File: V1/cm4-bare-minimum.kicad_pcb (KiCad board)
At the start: 2 copper layers, 120 x 120 mm, 59 parts, among them J1 Molex 470531000, J2 USB_OTG, J3 THD-02-R, J4 Micro_SD_Card_Det, J5 USB4105-GF-A, J6 Conn_01x03, J7 Conn_01x03, J8 THD-20-R, J9 MDT320M03001, U1 TPD2EUSB30, U2 EMC2301-1-ACZL-TR, U3 MagJack-A70-112-331N126, U4 RT9742GGJ5, U5 74LVC1G07SE-7, U6 MP1470

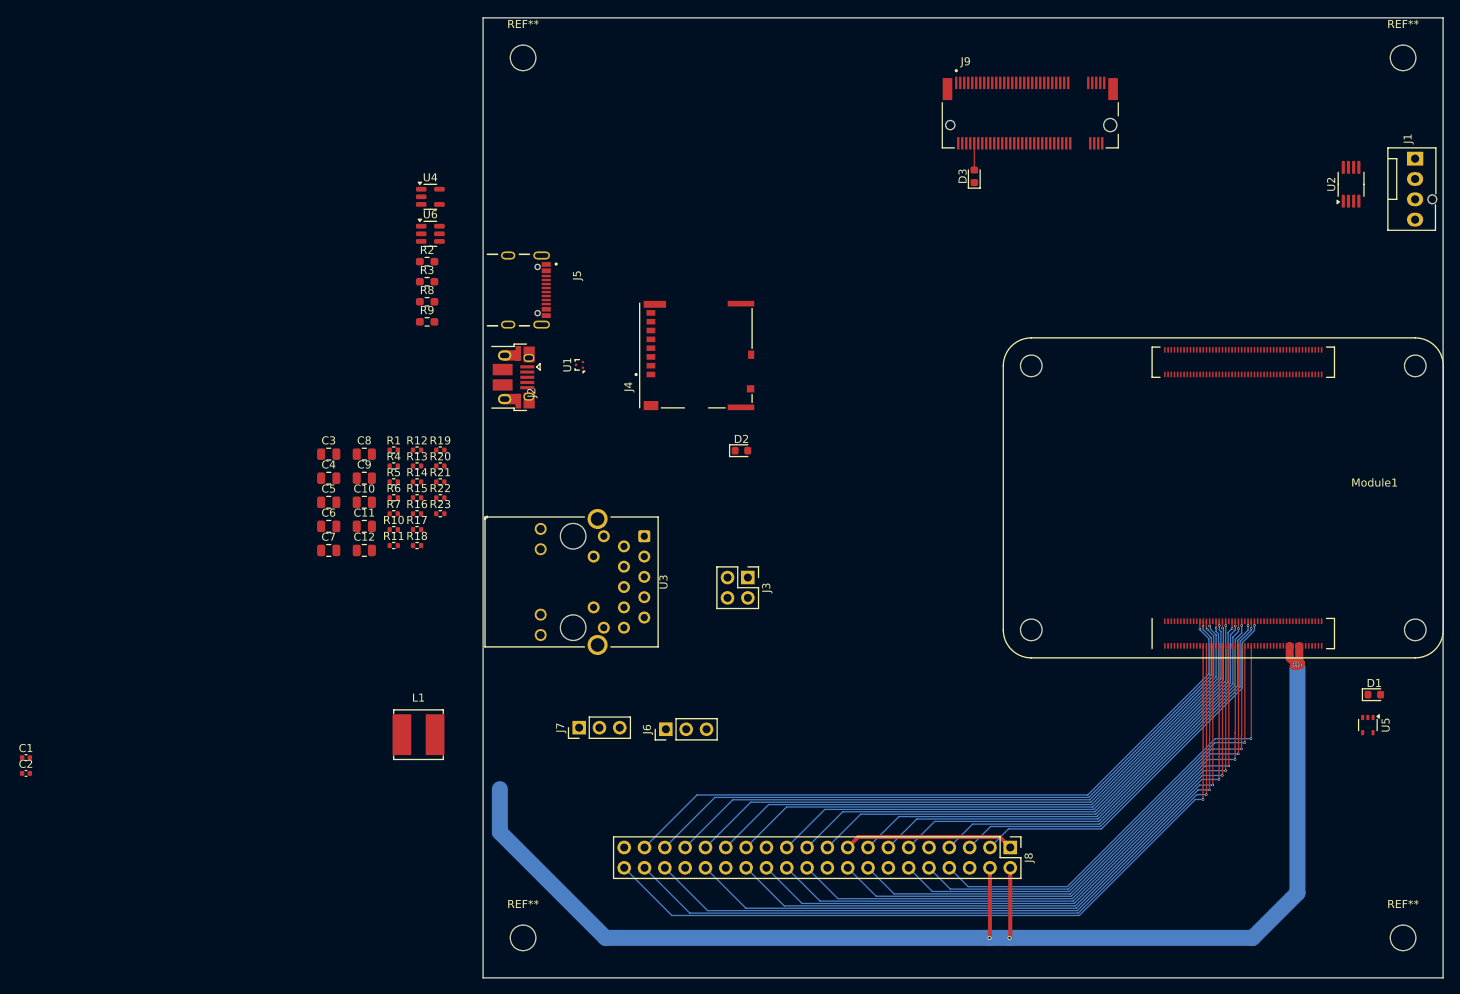
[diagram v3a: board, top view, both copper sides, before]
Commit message: Housekeeping, board size 120mmx40mm
V1 requirements are fulfilled, Connections are remaining in PCB layout, Performed Cleanup of repo so it only has the V1 Project.
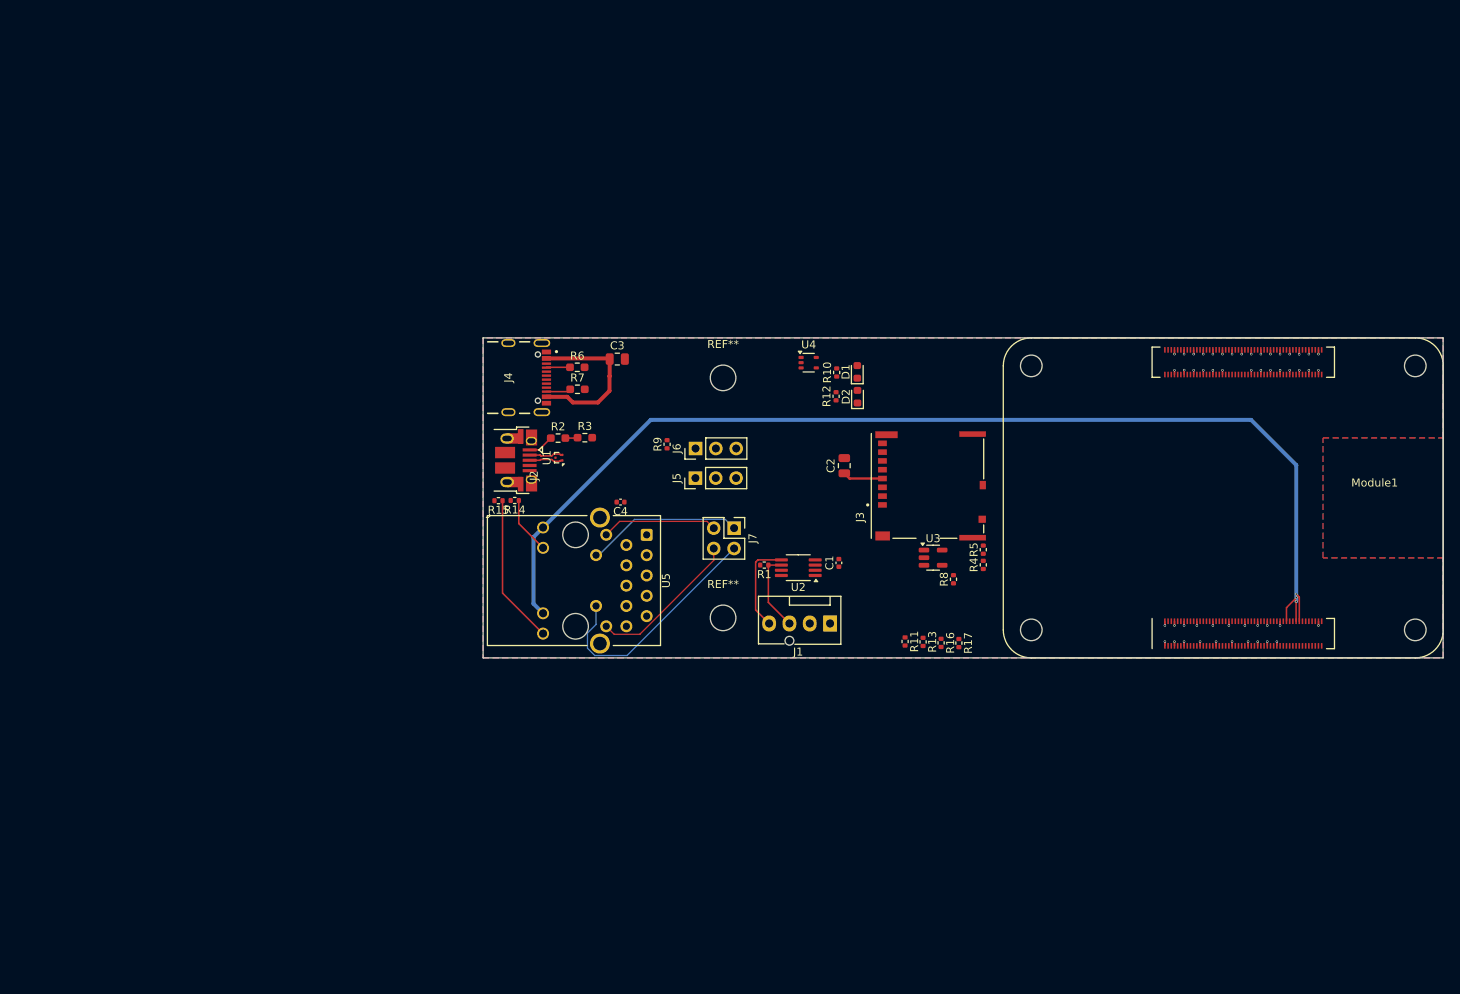
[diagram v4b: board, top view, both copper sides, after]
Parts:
- removed C10, C12, C6: 10u, Capacitor_SMD:C_0805_2012Metric
- removed C11, C7: 0.1u, Capacitor_SMD:C_0805_2012Metric
- removed C5: 13p, Capacitor_SMD:C_0805_2012Metric
- removed C8: 1u, Capacitor_SMD:C_0805_2012Metric
- removed C9: 10p, Capacitor_SMD:C_0805_2012Metric
- removed D3: LED Red, LED_SMD:LED_0603_1608Metric
- removed J8: THD-20-R, Connector_PinHeader_2.54mm:PinHeader_2x20_P2.54mm_Vertical
- removed J9: MDT320M03001, MDT320M03001:AMPHENOL_MDT320M03001
- removed L1: SRN6045TA-4R7Y, Inductor_SMD:L_Bourns_SRN6045TA
- removed R18: NC, Resistor_SMD:R_0402_1005Metric
- removed R19: 10, Resistor_SMD:R_0402_1005Metric
- removed R20: 40.2k, Resistor_SMD:R_0402_1005Metric
- removed R21: 100k, Resistor_SMD:R_0402_1005Metric
- removed R22: 20k, Resistor_SMD:R_0402_1005Metric
- removed R23: 13k, Resistor_SMD:R_0402_1005Metric
- removed the REF** at (205.0, 155.0)
- removed the REF** at (95.0, 45.0)
- removed U6: MP1470, Package_TO_SOT_SMD:TSOT-23-6
- C2: value 100n -> 10u; footprint Capacitor_SMD:C_0402_1005Metric -> Capacitor_SMD:C_0805_2012Metric
- C4: value 1u -> 100n; footprint Capacitor_SMD:C_0805_2012Metric -> Capacitor_SMD:C_0402_1005Metric
- J3: value THD-02-R -> Micro_SD_Card_Det; footprint Connector_PinHeader_2.54mm:PinHeader_2x02_P2.54mm_Vertical -> CM4IO:SDCARD_MOLEX_503398-1892
- J4: value Micro_SD_Card_Det -> USB4105-GF-A; footprint CM4IO:SDCARD_MOLEX_503398-1892 -> USB4105-GF-A:GCT_USB4105-GF-A
- J5: value USB4105-GF-A -> Conn_01x03; footprint USB4105-GF-A:GCT_USB4105-GF-A -> Connector_PinHeader_2.54mm:PinHeader_1x03_P2.54mm_Vertical
- J7: value Conn_01x03 -> THD-02-R; footprint Connector_PinHeader_2.54mm:PinHeader_1x03_P2.54mm_Vertical -> Connector_PinHeader_2.54mm:PinHeader_2x02_P2.54mm_Vertical
- R10: value 12K 1% -> 1k
- R13: value 1k -> NC
- R14: value NC -> 470R
- R15: value 1k -> 470R
- R4, R5: value 470R -> NC
- R6, R7: value NC -> 5.1k; footprint Resistor_SMD:R_0402_1005Metric -> Resistor_SMD:R_0603_1608Metric_Pad0.98x0.95mm_HandSolder
- R8: value 5.1k -> 12K 1%; footprint Resistor_SMD:R_0603_1608Metric_Pad0.98x0.95mm_HandSolder -> Resistor_SMD:R_0402_1005Metric
- R9: value 5.1k -> NC; footprint Resistor_SMD:R_0603_1608Metric_Pad0.98x0.95mm_HandSolder -> Resistor_SMD:R_0402_1005Metric
- U3: value MagJack-A70-112-331N126 -> RT9742GGJ5; footprint CM4IO:TRJG0926HENL -> Package_TO_SOT_SMD:SOT-23-5
- U4: value RT9742GGJ5 -> 74LVC1G07SE-7; footprint Package_TO_SOT_SMD:SOT-23-5 -> Package_TO_SOT_SMD:SOT-353_SC-70-5
- U5: value 74LVC1G07SE-7 -> MagJack-A70-112-331N126; footprint Package_TO_SOT_SMD:SOT-353_SC-70-5 -> CM4IO:TRJG0926HENL
- moved C2 109.3 mm to (135.2, 96.0), turned to 90 degrees
- moved C1 104.5 mm to (134.5, 108.1), turned to 90 degrees
- moved U5 100.7 mm to (101.6, 110.3)
- moved REF** 93.9 mm to (120.0, 85.0)
- moved J1 93.4 mm to (133.4, 115.7), turned to 180 degrees
- moved U2 84.1 mm to (129.4, 108.7), turned to 180 degrees
- moved D1 76.2 mm to (136.8, 84.2), turned to 90 degrees
- moved R4 74.7 mm to (152.5, 108.4), turned to 90 degrees
- moved R8 74.4 mm to (148.8, 110.2), turned to 90 degrees
- moved R5 74.2 mm to (152.5, 106.5), turned to 90 degrees
- moved R17 69.2 mm to (149.5, 118.2), turned to -90 degrees
- moved R16 67.5 mm to (147.2, 118.1), turned to -90 degrees
- moved R13 67.0 mm to (145.0, 118.0), turned to -90 degrees
- moved R11 65.0 mm to (142.8, 118.0), turned to -90 degrees
- moved R10 58.7 mm to (134.2, 84.3), turned to 90 degrees
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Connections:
- C2 pad 1: Net-(C2-Pad1) -> /SD_PWR
- C3 pad 1: /SD_PWR -> /CM4_5V
- C4 pad 2: Net-(U6-SW) -> GND
- D1 pad 2: /PWR_3V3 -> /CM4_3V3
- D2 pad 2: /PWR_3V3 -> /CM4_3V3
- J3 pad 1: /TR1_TAP -> /SD_DAT2
- J3 pad 2: /TR2_TAP -> /SD_DAT3
- J3 pad 3: /TR0_TAP -> /SD_CMD
- J3 pad 4: /TR3_TAP -> /SD_PWR
- J6 pad 1: /Global_EN -> Net-(J6-Pin_1)
- J6 pad 2: GND -> /nRPIBOOT
- J6 pad 3: /RUN_PG -> GND
- J7 pad 1: Net-(J7-Pin_1) -> /TR1_TAP
- J7 pad 2: /nRPIBOOT -> /TR2_TAP
- J7 pad 3: GND -> /TR0_TAP
- Module1 pad 102: /PCIe_CLK_nREQ -> unconnected-(Module1B-PCIe_CLK_nREQ-Pad102)
- Module1 pad 109: /PCIe_nRST -> unconnected-(Module1B-PCIe_nRST-Pad109)
- Module1 pad 110: /PCIe_CLK_P -> unconnected-(Module1B-PCIe_CLK_P-Pad110)
- Module1 pad 112: /PCIe_CLK_N -> unconnected-(Module1B-PCIe_CLK_N-Pad112)
- Module1 pad 116: /PCIe_RX_P -> unconnected-(Module1B-PCIe_RX_P-Pad116)
- Module1 pad 118: /PCIe_RX_N -> unconnected-(Module1B-PCIe_RX_N-Pad118)
- Module1 pad 122: /PCIe_TX_P -> unconnected-(Module1B-PCIe_TX_P-Pad122)
- Module1 pad 124: /PCIe_TX_N -> unconnected-(Module1B-PCIe_TX_N-Pad124)
- Module1 pad 24: /GPIO26 -> unconnected-(Module1A-GPIO26-Pad24)
- Module1 pad 25: /GPIO21 -> unconnected-(Module1A-GPIO21-Pad25)
- Module1 pad 26: /GPIO19 -> unconnected-(Module1A-GPIO19-Pad26)
- Module1 pad 27: /GPIO20 -> unconnected-(Module1A-GPIO20-Pad27)
- Module1 pad 28: /GPIO13 -> unconnected-(Module1A-GPIO13-Pad28)
- Module1 pad 29: /GPIO16 -> unconnected-(Module1A-GPIO16-Pad29)
- Module1 pad 30: /GPIO6 -> unconnected-(Module1A-GPIO6-Pad30)
- Module1 pad 31: /GPIO12 -> unconnected-(Module1A-GPIO12-Pad31)
- Module1 pad 34: /GPIO5 -> unconnected-(Module1A-GPIO5-Pad34)
- Module1 pad 35: /ID_SC -> unconnected-(Module1A-ID_SC-Pad35)
- Module1 pad 36: /ID_SD -> unconnected-(Module1A-ID_SD-Pad36)
- Module1 pad 37: /GPIO7 -> unconnected-(Module1A-GPIO7-Pad37)
- Module1 pad 38: /GPIO11 -> unconnected-(Module1A-GPIO11-Pad38)
- Module1 pad 39: /GPIO8 -> unconnected-(Module1A-GPIO8-Pad39)
- Module1 pad 40: /GPIO9 -> unconnected-(Module1A-GPIO9-Pad40)
- Module1 pad 41: /GPIO25 -> unconnected-(Module1A-GPIO25-Pad41)
- Module1 pad 44: /GPIO10 -> unconnected-(Module1A-GPIO10-Pad44)
- Module1 pad 45: /GPIO24 -> unconnected-(Module1A-GPIO24-Pad45)
- Module1 pad 46: /GPIO22 -> unconnected-(Module1A-GPIO22-Pad46)
- Module1 pad 47: /GPIO23 -> unconnected-(Module1A-GPIO23-Pad47)
- Module1 pad 48: /GPIO27 -> unconnected-(Module1A-GPIO27-Pad48)
- Module1 pad 49: /GPIO18 -> unconnected-(Module1A-GPIO18-Pad49)
- Module1 pad 50: /GPIO17 -> unconnected-(Module1A-GPIO17-Pad50)
- Module1 pad 51: /GPIO15 -> unconnected-(Module1A-GPIO15-Pad51)
- Module1 pad 54: /GPIO4 -> unconnected-(Module1A-GPIO4-Pad54)
- Module1 pad 55: /GPIO14 -> unconnected-(Module1A-GPIO14-Pad55)
- Module1 pad 56: /GPIO3 -> unconnected-(Module1A-GPIO3-Pad56)
- Module1 pad 58: /GPIO2 -> unconnected-(Module1A-GPIO2-Pad58)
- Module1 pad 94: /AnalogIP1 -> unconnected-(Module1A-AnalogIP1-Pad94)
- Module1 pad 96: /AnalogIP0 -> unconnected-(Module1A-AnalogIP0-Pad96)
- R1 pad 2: /PWR_3V3 -> /CM4_3V3
- R10 pad 1: /CM4_3V3 -> Net-(D1-K)
- R10 pad 2: /SD_PWR_ON -> Net-(R10-Pad2)
- R11 pad 1: Net-(J7-Pin_1) -> /SD_VDD_Override
- R11 pad 2: /CM4_3V3 -> GND
- R12 pad 1: /PWR_3V3 -> Net-(D2-K)
- R12 pad 2: /LED1 -> /PI_nLED_Activity
- R13 pad 1: Net-(D1-K) -> /EEPROM_nWP
- R13 pad 2: Net-(R13-Pad2) -> GND
- R14 pad 1: /SD_VDD_Override -> Net-(U5-LEDG_K)
- R14 pad 2: GND -> /ETH_LEDG
- R15 pad 1: Net-(D2-K) -> Net-(U5-LEDY_K)
- R15 pad 2: /PI_nLED_Activity -> /ETH_LEDY
- R16 pad 1: /EEPROM_nWP -> /BT_nDisable
- R17 pad 1: /BT_nDisable -> /WiFi_nDisable
- R4 pad 1: Net-(U3-LEDG_K) -> /CM4_3V3
- R4 pad 2: /ETH_LEDG -> Net-(J3-DET_A)
- R5 pad 1: Net-(U3-LEDY_K) -> /Reserved
- R5 pad 2: /ETH_LEDY -> Net-(J3-DET_B)
- R6 pad 1: /CM4_3V3 -> Net-(J4-CC1)
- R6 pad 2: Net-(J4-DET_A) -> GND
- R7 pad 1: /Reserved -> Net-(J4-CC2)
- R7 pad 2: Net-(J4-DET_B) -> GND
- R8 pad 1: Net-(J5-CC1) -> /CM4_3V3
- R8 pad 2: GND -> /SD_PWR_ON
- R9 pad 1: Net-(J5-CC2) -> Net-(J6-Pin_1)
- R9 pad 2: GND -> /CM4_3V3
- U3 pad 1: unconnected-(U3-TRD0+-Pad1) -> /SD_PWR
- U3 pad 2: /TRD0_N -> GND
- U3 pad 3: /TRD1_P -> unconnected-(U3-nFLG-Pad3)
- U3 pad 4: Net-(C2-Pad1) -> /SD_PWR_ON
- U3 pad 5: Net-(C2-Pad1) -> /CM4_3V3
- U4 pad 1: /SD_PWR -> (no net)
- U4 pad 2: GND -> /nPI_LED_PWR
- U4 pad 3: unconnected-(U4-nFLG-Pad3) -> GND
- U4 pad 4: /SD_PWR_ON -> Net-(R10-Pad2)
- U5 pad 1: (no net) -> /TRD0_P
- U5 pad 2: /nPI_LED_PWR -> /TRD0_N
- U5 pad 3: GND -> /TRD1_P
- U5 pad 4: Net-(R13-Pad2) -> Net-(C4-Pad1)
- U5 pad 5: /CM4_3V3 -> Net-(C4-Pad1)
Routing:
- net /CM4_5V: track 165.2 -> 20.7 mm, vias 7 -> 0
- net /CM4_3V3: track 21.4 -> 140.3 mm, vias 0 -> 3
- net /GPIO21: track 100.0 -> 0.00 mm, vias 1 -> 0
- net /GPIO20: track 97.3 -> 0.00 mm, vias 1 -> 0
- net /GPIO16: track 94.6 -> 0.00 mm, vias 1 -> 0
- net /GPIO12: track 89.3 -> 0.00 mm, vias 1 -> 0
- net /GPIO26: track 86.6 -> 0.00 mm, vias 1 -> 0
- net /GPIO19: track 84.4 -> 0.00 mm, vias 1 -> 0
- net /ID_SC: track 84.3 -> 0.00 mm, vias 1 -> 0
- net /GPIO13: track 82.2 -> 0.00 mm, vias 1 -> 0
- net /GPIO7: track 81.7 -> 0.00 mm, vias 1 -> 0
- net /GPIO6: track 80.0 -> 0.00 mm, vias 1 -> 0
- net /GPIO8: track 78.9 -> 0.00 mm, vias 1 -> 0
- net /GPIO5: track 77.6 -> 0.00 mm, vias 1 -> 0
- net /GPIO25: track 76.2 -> 0.00 mm, vias 1 -> 0
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- added copper zone on B.Cu, net GND
- added copper zone on F.Cu, net GND
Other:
- board size 120 x 120 mm -> 120 x 40 mm

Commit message: Updated PCB layout
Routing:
- net /CM4_5V: track 20.7 -> 139.1 mm, vias 0 -> 7
- net /USB2_P: track 4.26 -> 86.0 mm, vias 0 -> 2
- net /USB2_N: track 4.26 -> 85.2 mm, vias 0 -> 2
- net /USB_OTG_ID: track 1.55 -> 78.3 mm, vias 0 -> 2
- net /CM4_3V3: track 140.3 -> 160.3 mm, vias 3 -> 6
- net /SD_PWR: track 5.05 -> 16.6 mm
- net Net-(J3-DET_A): track 0.00 -> 10.2 mm
- net /RUN_PG: track 0.00 -> 7.75 mm
- net /SCL0: track 0.00 -> 6.03 mm, vias 0 -> 2
- net /SDA0: track 0.00 -> 5.75 mm, vias 0 -> 2
- net /Reserved: track 0.00 -> 5.17 mm
- net GND: track 27.1 -> 31.4 mm, vias 51 -> 55
- net Net-(J3-DET_B): track 0.00 -> 3.95 mm
- net Net-(J6-Pin_1): track 0.00 -> 3.57 mm
- net Net-(D2-K): track 0.00 -> 2.81 mm
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
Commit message: Updated PCB layout
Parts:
- added C10: 10u, Capacitor_SMD:C_0805_2012Metric, F.Cu at (75.2, 100.5)
- added C11: 0.1u, Capacitor_SMD:C_0805_2012Metric, F.Cu at (75.2, 103.6)
- added C12: 10u, Capacitor_SMD:C_0805_2012Metric, F.Cu at (75.2, 106.6)
- added C5: 13p, Capacitor_SMD:C_0805_2012Metric, F.Cu at (70.7, 100.5)
- added C6: 10u, Capacitor_SMD:C_0805_2012Metric, F.Cu at (70.7, 103.6)
- added C7: 0.1u, Capacitor_SMD:C_0805_2012Metric, F.Cu at (70.7, 106.6)
- added C8: 1u, Capacitor_SMD:C_0805_2012Metric, F.Cu at (75.2, 94.5)
- added C9: 10p, Capacitor_SMD:C_0805_2012Metric, F.Cu at (75.2, 97.5)
- added D3: LED Red, LED_SMD:LED_0603_1608Metric, F.Cu at (151.4, 59.8)
- added J8: THD-20-R, Connector_PinHeader_2.54mm:PinHeader_2x20_P2.54mm_Vertical, F.Cu at (155.9, 143.7)
- added J9: MDT320M03001, MDT320M03001:AMPHENOL_MDT320M03001, F.Cu at (158.4, 53.4)
- added L1: SRN6045TA-4R7Y, Inductor_SMD:L_Bourns_SRN6045TA, F.Cu at (81.9, 129.6)
- added R18: NC, Resistor_SMD:R_0402_1005Metric, F.Cu at (81.7, 106.0)
- added R19: 10, Resistor_SMD:R_0402_1005Metric, F.Cu at (84.7, 94.0)
- added R20: 40.2k, Resistor_SMD:R_0402_1005Metric, F.Cu at (84.7, 96.0)
- added R21: 100k, Resistor_SMD:R_0402_1005Metric, F.Cu at (84.7, 98.0)
- added R22: 20k, Resistor_SMD:R_0402_1005Metric, F.Cu at (84.7, 100.0)
- added R23: 13k, Resistor_SMD:R_0402_1005Metric, F.Cu at (84.7, 102.0)
- added REF**: MountingHole_3.2mm_M3, MountingHole:MountingHole_3.2mm_M3, F.Cu at (205.0, 155.0)
- added REF**: MountingHole_3.2mm_M3, MountingHole:MountingHole_3.2mm_M3, F.Cu at (95.0, 45.0)
- added U6: MP1470, Package_TO_SOT_SMD:TSOT-23-6, F.Cu at (83.4, 67.0)
- C2: value 10u -> 100n; footprint Capacitor_SMD:C_0805_2012Metric -> Capacitor_SMD:C_0402_1005Metric
- C4: value 100n -> 1u; footprint Capacitor_SMD:C_0402_1005Metric -> Capacitor_SMD:C_0805_2012Metric
- J3: value Micro_SD_Card_Det -> THD-02-R; footprint CM4IO:SDCARD_MOLEX_503398-1892 -> Connector_PinHeader_2.54mm:PinHeader_2x02_P2.54mm_Vertical
- J4: value USB4105-GF-A -> Micro_SD_Card_Det; footprint USB4105-GF-A:GCT_USB4105-GF-A -> CM4IO:SDCARD_MOLEX_503398-1892
- J5: value Conn_01x03 -> USB4105-GF-A; footprint Connector_PinHeader_2.54mm:PinHeader_1x03_P2.54mm_Vertical -> USB4105-GF-A:GCT_USB4105-GF-A
- J7: value THD-02-R -> Conn_01x03; footprint Connector_PinHeader_2.54mm:PinHeader_2x02_P2.54mm_Vertical -> Connector_PinHeader_2.54mm:PinHeader_1x03_P2.54mm_Vertical
- R10: value 1k -> 12K 1%
- R13: value NC -> 1k
- R14: value 470R -> NC
- R15: value 470R -> 1k
- R4, R5: value NC -> 470R
- R6, R7: value 5.1k -> NC; footprint Resistor_SMD:R_0603_1608Metric_Pad0.98x0.95mm_HandSolder -> Resistor_SMD:R_0402_1005Metric
- R8: value 12K 1% -> 5.1k; footprint Resistor_SMD:R_0402_1005Metric -> Resistor_SMD:R_0603_1608Metric_Pad0.98x0.95mm_HandSolder
- R9: value NC -> 5.1k; footprint Resistor_SMD:R_0402_1005Metric -> Resistor_SMD:R_0603_1608Metric_Pad0.98x0.95mm_HandSolder
- U3: value RT9742GGJ5 -> MagJack-A70-112-331N126; footprint Package_TO_SOT_SMD:SOT-23-5 -> CM4IO:TRJG0926HENL
- U4: value 74LVC1G07SE-7 -> RT9742GGJ5; footprint Package_TO_SOT_SMD:SOT-353_SC-70-5 -> Package_TO_SOT_SMD:SOT-23-5
- U5: value MagJack-A70-112-331N126 -> 74LVC1G07SE-7; footprint CM4IO:TRJG0926HENL -> Package_TO_SOT_SMD:SOT-353_SC-70-5
- moved C2 109.3 mm to (32.9, 134.4), turned to 0 degrees
- moved C1 104.5 mm to (32.9, 132.5), turned to 0 degrees
- moved U5 100.7 mm to (200.6, 128.4)
- moved REF** 93.9 mm to (205.0, 45.0)
- moved J1 93.4 mm to (206.5, 57.6), turned to -90 degrees
- moved U2 84.1 mm to (198.5, 60.8), turned to 90 degrees
- moved D1 76.2 mm to (201.4, 124.6), turned to 0 degrees
- moved R4 74.7 mm to (78.8, 96.0), turned to 0 degrees
- moved R8 74.4 mm to (83.0, 75.5), turned to 0 degrees
- moved R5 74.2 mm to (78.8, 98.0), turned to 0 degrees
- moved R17 69.2 mm to (81.7, 104.0), turned to 0 degrees
- moved R16 67.5 mm to (81.7, 102.0), turned to 0 degrees
- moved R13 67.0 mm to (81.7, 96.0), turned to 0 degrees
- moved R11 65.0 mm to (78.8, 106.0), turned to 0 degrees
- moved R10 58.7 mm to (78.8, 104.0), turned to 0 degrees
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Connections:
- C2 pad 1: /SD_PWR -> Net-(C2-Pad1)
- C3 pad 1: /CM4_5V -> /SD_PWR
- C4 pad 2: GND -> Net-(U6-SW)
- D1 pad 2: /CM4_3V3 -> /PWR_3V3
- D2 pad 2: /CM4_3V3 -> /PWR_3V3
- J3 pad 1: /SD_DAT2 -> /TR1_TAP
- J3 pad 2: /SD_DAT3 -> /TR2_TAP
- J3 pad 3: /SD_CMD -> /TR0_TAP
- J3 pad 4: /SD_PWR -> /TR3_TAP
- J6 pad 1: Net-(J6-Pin_1) -> /Global_EN
- J6 pad 2: /nRPIBOOT -> GND
- J6 pad 3: GND -> /RUN_PG
- J7 pad 1: /TR1_TAP -> Net-(J7-Pin_1)
- J7 pad 2: /TR2_TAP -> /nRPIBOOT
- J7 pad 3: /TR0_TAP -> GND
- Module1 pad 102: unconnected-(Module1B-PCIe_CLK_nREQ-Pad102) -> /PCIe_CLK_nREQ
- Module1 pad 109: unconnected-(Module1B-PCIe_nRST-Pad109) -> /PCIe_nRST
- Module1 pad 110: unconnected-(Module1B-PCIe_CLK_P-Pad110) -> /PCIe_CLK_P
- Module1 pad 112: unconnected-(Module1B-PCIe_CLK_N-Pad112) -> /PCIe_CLK_N
- Module1 pad 116: unconnected-(Module1B-PCIe_RX_P-Pad116) -> /PCIe_RX_P
- Module1 pad 118: unconnected-(Module1B-PCIe_RX_N-Pad118) -> /PCIe_RX_N
- Module1 pad 122: unconnected-(Module1B-PCIe_TX_P-Pad122) -> /PCIe_TX_P
- Module1 pad 124: unconnected-(Module1B-PCIe_TX_N-Pad124) -> /PCIe_TX_N
- Module1 pad 24: unconnected-(Module1A-GPIO26-Pad24) -> /GPIO26
- Module1 pad 25: unconnected-(Module1A-GPIO21-Pad25) -> /GPIO21
- Module1 pad 26: unconnected-(Module1A-GPIO19-Pad26) -> /GPIO19
- Module1 pad 27: unconnected-(Module1A-GPIO20-Pad27) -> /GPIO20
- Module1 pad 28: unconnected-(Module1A-GPIO13-Pad28) -> /GPIO13
- Module1 pad 29: unconnected-(Module1A-GPIO16-Pad29) -> /GPIO16
- Module1 pad 30: unconnected-(Module1A-GPIO6-Pad30) -> /GPIO6
- Module1 pad 31: unconnected-(Module1A-GPIO12-Pad31) -> /GPIO12
- Module1 pad 34: unconnected-(Module1A-GPIO5-Pad34) -> /GPIO5
- Module1 pad 35: unconnected-(Module1A-ID_SC-Pad35) -> /ID_SC
- Module1 pad 36: unconnected-(Module1A-ID_SD-Pad36) -> /ID_SD
- Module1 pad 37: unconnected-(Module1A-GPIO7-Pad37) -> /GPIO7
- Module1 pad 38: unconnected-(Module1A-GPIO11-Pad38) -> /GPIO11
- Module1 pad 39: unconnected-(Module1A-GPIO8-Pad39) -> /GPIO8
- Module1 pad 40: unconnected-(Module1A-GPIO9-Pad40) -> /GPIO9
- Module1 pad 41: unconnected-(Module1A-GPIO25-Pad41) -> /GPIO25
- Module1 pad 44: unconnected-(Module1A-GPIO10-Pad44) -> /GPIO10
- Module1 pad 45: unconnected-(Module1A-GPIO24-Pad45) -> /GPIO24
- Module1 pad 46: unconnected-(Module1A-GPIO22-Pad46) -> /GPIO22
- Module1 pad 47: unconnected-(Module1A-GPIO23-Pad47) -> /GPIO23
- Module1 pad 48: unconnected-(Module1A-GPIO27-Pad48) -> /GPIO27
- Module1 pad 49: unconnected-(Module1A-GPIO18-Pad49) -> /GPIO18
- Module1 pad 50: unconnected-(Module1A-GPIO17-Pad50) -> /GPIO17
- Module1 pad 51: unconnected-(Module1A-GPIO15-Pad51) -> /GPIO15
- Module1 pad 54: unconnected-(Module1A-GPIO4-Pad54) -> /GPIO4
- Module1 pad 55: unconnected-(Module1A-GPIO14-Pad55) -> /GPIO14
- Module1 pad 56: unconnected-(Module1A-GPIO3-Pad56) -> /GPIO3
- Module1 pad 58: unconnected-(Module1A-GPIO2-Pad58) -> /GPIO2
- Module1 pad 94: unconnected-(Module1A-AnalogIP1-Pad94) -> /AnalogIP1
- Module1 pad 96: unconnected-(Module1A-AnalogIP0-Pad96) -> /AnalogIP0
- R1 pad 2: /CM4_3V3 -> /PWR_3V3
- R10 pad 1: Net-(D1-K) -> /CM4_3V3
- R10 pad 2: Net-(R10-Pad2) -> /SD_PWR_ON
- R11 pad 1: /SD_VDD_Override -> Net-(J7-Pin_1)
- R11 pad 2: GND -> /CM4_3V3
- R12 pad 1: Net-(D2-K) -> /PWR_3V3
- R12 pad 2: /PI_nLED_Activity -> /LED1
- R13 pad 1: /EEPROM_nWP -> Net-(D1-K)
- R13 pad 2: GND -> Net-(R13-Pad2)
- R14 pad 1: Net-(U5-LEDG_K) -> /SD_VDD_Override
- R14 pad 2: /ETH_LEDG -> GND
- R15 pad 1: Net-(U5-LEDY_K) -> Net-(D2-K)
- R15 pad 2: /ETH_LEDY -> /PI_nLED_Activity
- R16 pad 1: /BT_nDisable -> /EEPROM_nWP
- R17 pad 1: /WiFi_nDisable -> /BT_nDisable
- R4 pad 1: /CM4_3V3 -> Net-(U3-LEDG_K)
- R4 pad 2: Net-(J3-DET_A) -> /ETH_LEDG
- R5 pad 1: /Reserved -> Net-(U3-LEDY_K)
- R5 pad 2: Net-(J3-DET_B) -> /ETH_LEDY
- R6 pad 1: Net-(J4-CC1) -> /CM4_3V3
- R6 pad 2: GND -> Net-(J4-DET_A)
- R7 pad 1: Net-(J4-CC2) -> /Reserved
- R7 pad 2: GND -> Net-(J4-DET_B)
- R8 pad 1: /CM4_3V3 -> Net-(J5-CC1)
- R8 pad 2: /SD_PWR_ON -> GND
- R9 pad 1: Net-(J6-Pin_1) -> Net-(J5-CC2)
- R9 pad 2: /CM4_3V3 -> GND
- U3 pad 1: /SD_PWR -> unconnected-(U3-TRD0+-Pad1)
- U3 pad 2: GND -> /TRD0_N
- U3 pad 3: unconnected-(U3-nFLG-Pad3) -> /TRD1_P
- U3 pad 4: /SD_PWR_ON -> Net-(C2-Pad1)
- U3 pad 5: /CM4_3V3 -> Net-(C2-Pad1)
- U4 pad 1: (no net) -> /SD_PWR
- U4 pad 2: /nPI_LED_PWR -> GND
- U4 pad 3: GND -> unconnected-(U4-nFLG-Pad3)
- U4 pad 4: Net-(R10-Pad2) -> /SD_PWR_ON
- U5 pad 1: /TRD0_P -> (no net)
- U5 pad 2: /TRD0_N -> /nPI_LED_PWR
- U5 pad 3: /TRD1_P -> GND
- U5 pad 4: Net-(C4-Pad1) -> Net-(R13-Pad2)
- U5 pad 5: Net-(C4-Pad1) -> /CM4_3V3
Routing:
- net /CM4_3V3: track 160.3 -> 21.4 mm, vias 6 -> 0
- net /GPIO21: track 0.00 -> 100.0 mm, vias 0 -> 1
- net /GPIO20: track 0.00 -> 97.3 mm, vias 0 -> 1
- net /GPIO16: track 0.00 -> 94.6 mm, vias 0 -> 1
- net /GPIO12: track 0.00 -> 89.3 mm, vias 0 -> 1
- net /GPIO26: track 0.00 -> 86.6 mm, vias 0 -> 1
- net /GPIO19: track 0.00 -> 84.4 mm, vias 0 -> 1
- net /ID_SC: track 0.00 -> 84.3 mm, vias 0 -> 1
- net /GPIO13: track 0.00 -> 82.2 mm, vias 0 -> 1
- net /GPIO7: track 0.00 -> 81.7 mm, vias 0 -> 1
- net /GPIO6: track 0.00 -> 80.0 mm, vias 0 -> 1
- net /GPIO8: track 0.00 -> 78.9 mm, vias 0 -> 1
- net /USB_OTG_ID: track 78.3 -> 0.00 mm, vias 2 -> 0
- net /GPIO5: track 0.00 -> 77.6 mm, vias 0 -> 1
- net /GPIO25: track 0.00 -> 76.2 mm, vias 0 -> 1
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- removed copper zone on B.Cu, net GND
- removed copper zone on F.Cu, net GND
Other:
- board size 120 x 40 mm -> 120 x 120 mm
